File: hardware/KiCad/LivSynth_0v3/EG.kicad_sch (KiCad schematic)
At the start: 27 parts, among them J11 Jumper, Q10 2N3904, Q13 2N3904, Q15 2N3904, Q2 2N3904, SW2 SW_SPST, U5 TL074

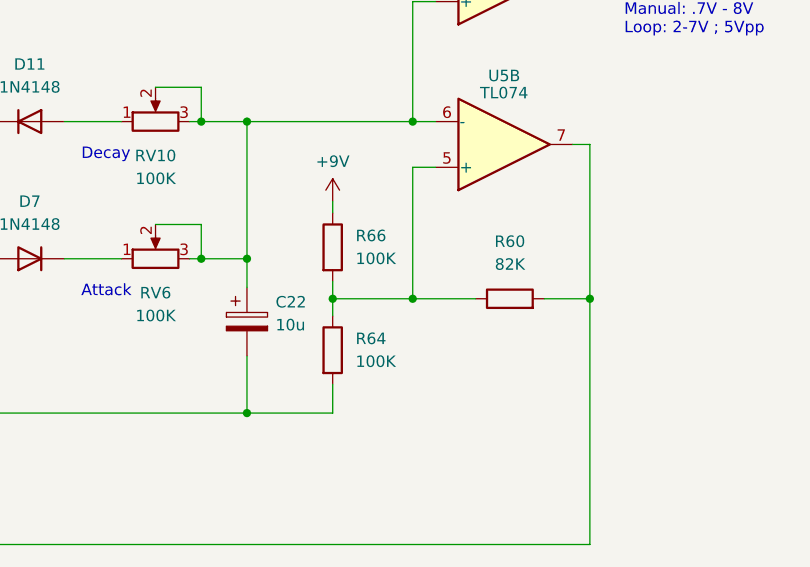
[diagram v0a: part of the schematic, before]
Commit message: Add another LFO cap for easier modding please MCU connectors to the backside Relocate reset button KiCad 7.0.1
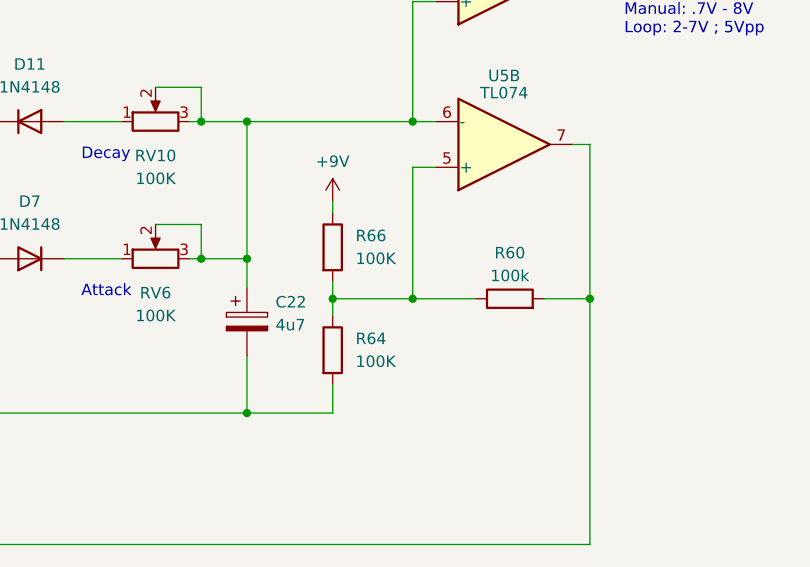
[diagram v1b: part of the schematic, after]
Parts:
- C22: value 10u -> 4u7
- R60: value 82K -> 100k
